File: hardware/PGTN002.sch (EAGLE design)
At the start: 25 parts, among them J1 DCJ0202DCJ0202

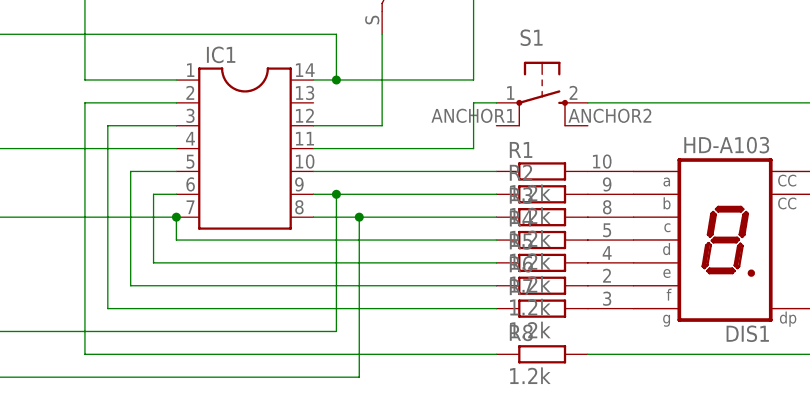
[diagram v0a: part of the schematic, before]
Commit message: Fixed MISO and SCK connection between ATTINY44 and ISP10 socket swapped
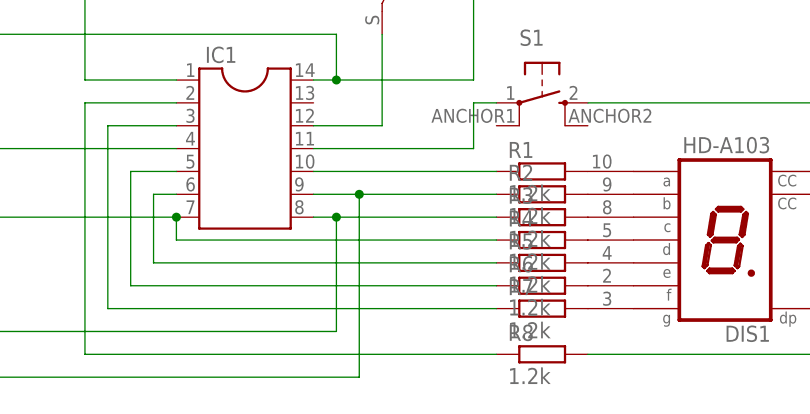
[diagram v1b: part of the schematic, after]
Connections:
- net N$10: now also IC1.8, R3.1; no longer IC1.9, R2.1
- net N$11: now also IC1.9, R2.1; no longer IC1.8, R3.1
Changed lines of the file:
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@@
 <grid distance="0.1" unitdist="inch" unit="inch" style="lines" multiple="1" display="no" altdistance="0.01" altunitdist="inch" altunit="inch"/>
 <layers>
-<layer number="1" name="Top" color="4" fill="1" visible="yes" active="no"/>
-<layer number="16" name="Bottom" color="1" fill="1" visible="yes" active="no"/>
-<layer number="17" name="Pads" color="2" fill="1" visible="yes" active="no"/>
-<layer number="18" name="Vias" color="2" fill="1" visible="yes" active="no"/>
-<layer number="19" name="Unrouted" color="6" fill="1" visible="yes" active="no"/>
-<layer number="20" name="Dimension" color="15" fill="1" visible="yes" active="no"/>
-<layer number="21" name="tPlace" color="7" fill="1" visible="yes" active="no"/>
-<layer number="22" name="bPlace" color="7" fill="1" visible="yes" active="no"/>
-<layer number="23" name="tOrigins" color="15" fill="1" visible="yes" active="no"/>
-<layer number="24" name="bOrigins" color="15" fill="1" visible="yes" active="no"/>
-<layer number="25" name="tNames" color="7" fill="1" visible="yes" active="no"/>
-<layer number="26" name="bNames" color="7" fill="1" visible="yes" active="no"/>
-<layer number="27" name="tValues" color="7" fill="1" visible="yes" active="no"/>
-<layer number="28" name="bValues" color="7" fill="1" visible="yes" active="no"/>
+<layer number="1" name="Top" color="4" fill="1" visible="no" active="no"/>
+<layer number="16" name="Bottom" color="1" fill="1" visible="no" active="no"/>
+<layer number="17" name="Pads" color="2" fill="1" visible="no" active="no"/>
+<layer number="18" name="Vias" color="2" fill="1" visible="no" active="no"/>
+<layer number="19" name="Unrouted" color="6" fill="1" visible="no" active="no"/>
+<layer number="20" name="Dimension" color="15" fill="1" visible="no" active="no"/>
+<layer number="21" name="tPlace" color="7" fill="1" visible="no" active="no"/>
+<layer number="22" name="bPlace" color="7" fill="1" visible="no" active="no"/>
+<layer number="23" name="tOrigins" color="15" fill="1" visible="no" active="no"/>
+<layer number="24" name="bOrigins" color="15" fill="1" visible="no" active="no"/>
+<layer number="25" name="tNames" color="7" fill="1" visible="no" active="no"/>
+<layer number="26" name="bNames" color="7" fill="1" visible="no" active="no"/>
+<layer number="27" name="tValues" color="7" fill="1" visible="no" active="no"/>
+<layer number="28" name="bValues" color="7" fill="1" visible="no" active="no"/>
 <layer number="29" name="tStop" color="7" fill="3" visible="no" active="no"/>
 <layer number="30" name="bStop" color="7" fill="6" visible="no" active="no"/>
@@
 <layer number="35" name="tGlue" color="7" fill="4" visible="no" active="no"/>
 <layer number="36" name="bGlue" color="7" fill="5" visible="no" active="no"/>
-<layer number="37" name="tTest" color="7" fill="1" visible="yes" active="no"/>
-<layer number="38" name="bTest" color="7" fill="1" visible="yes" active="no"/>
+<layer number="37" name="tTest" color="7" fill="1" visible="no" active="no"/>
+<layer number="38" name="bTest" color="7" fill="1" visible="no" active="no"/>
 <layer number="39" name="tKeepout" color="4" fill="11" visible="no" active="no"/>
 <layer number="40" name="bKeepout" color="1" fill="11" visible="no" active="no"/>
@@
 <layer number="44" name="Drills" color="7" fill="1" visible="no" active="no"/>
 <layer number="45" name="Holes" color="7" fill="1" visible="no" active="no"/>
-<layer number="46" name="Milling" color="3" fill="1" visible="yes" active="no"/>
-<layer number="47" name="Measures" color="7" fill="1" visible="yes" active="no"/>
-<layer number="48" name="Document" color="7" fill="1" visible="yes" active="no"/>
-<layer number="49" name="Reference" color="7" fill="1" visible="yes" active="no"/>
-<layer number="50" name="dxf" color="7" fill="1" visible="yes" active="no"/>
-<layer number="51" name="tDocu" color="7" fill="1" visible="yes" active="no"/>
-<layer number="52" name="bDocu" color="7" fill="1" visible="yes" active="no"/>
-<layer number="53" name="tGND_GNDA" color="7" fill="9" visible="yes" active="no"/>
-<layer number="54" name="bGND_GNDA" color="1" fill="9" visible="yes" active="no"/>
-<layer number="56" name="wert" color="7" fill="1" visible="yes" active="no"/>
+<layer number="46" name="Milling" color="3" fill="1" visible="no" active="no"/>
+<layer number="47" name="Measures" color="7" fill="1" visible="no" active="no"/>
+<layer number="48" name="Document" color="7" fill="1" visible="no" active="no"/>
+<layer number="49" name="Reference" color="7" fill="1" visible="no" active="no"/>
+<layer number="50" name="dxf" color="7" fill="1" visible="no" active="no"/>
+<layer number="51" name="tDocu" color="7" fill="1" visible="no" active="no"/>
+<layer number="52" name="bDocu" color="7" fill="1" visible="no" active="no"/>
+<layer number="53" name="tGND_GNDA" color="7" fill="9" visible="no" active="no"/>
+<layer number="54" name="bGND_GNDA" color="1" fill="9" visible="no" active="no"/>
+<layer number="56" name="wert" color="7" fill="1" visible="no" active="no"/>
 <layer number="91" name="Nets" color="2" fill="1" visible="yes" active="yes"/>
 <layer number="92" name="Busses" color="1" fill="1" visible="yes" active="yes"/>
@@
 <net name="N$10" class="0">
 <segment>
+<wire x1="10.16" y1="-7.62" x2="-30.48" y2="-7.62" width="0.1524" layer="91"/>
+<pinref part="MISO" gate="HEADER" pin="3"/>
+<pinref part="R3" gate="G$1" pin="1"/>
+<pinref part="IC1" gate="G$1" pin="8"/>
+<wire x1="7.62" y1="5.08" x2="10.16" y2="5.08" width="0.1524" layer="91"/>
+<wire x1="12.7" y1="5.08" x2="27.94" y2="5.08" width="0.1524" layer="91"/>
+<wire x1="10.16" y1="-7.62" x2="10.16" y2="5.08" width="0.1524" layer="91"/>
+<wire x1="10.16" y1="5.08" x2="12.7" y2="5.08" width="0.1524" layer="91"/>
+<junction x="10.16" y="5.08"/>
+</segment>
+</net>
+<net name="N$11" class="0">
+<segment>
+<wire x1="12.7" y1="-12.7" x2="-30.48" y2="-12.7" width="0.1524" layer="91"/>
+<pinref part="SCK" gate="HEADER" pin="3"/>
+<pinref part="R2" gate="G$1" pin="1"/>
 <pinref part="IC1" gate="G$1" pin="9"/>
-<wire x1="7.62" y1="7.62" x2="10.16" y2="7.62" width="0.1524" layer="91"/>
-<pinref part="R2" gate="G$1" pin="1"/>
-<wire x1="10.16" y1="7.62" x2="27.94" y2="7.62" width="0.1524" layer="91"/>
-<wire x1="10.16" y1="7.62" x2="10.16" y2="-7.62" width="0.1524" layer="91"/>
-<wire x1="10.16" y1="-7.62" x2="-30.48" y2="-7.62" width="0.1524" layer="91"/>
-<junction x="10.16" y="7.62"/>
-<pinref part="MISO" gate="HEADER" pin="3"/>
-</segment>
-</net>
-<net name="N$11" class="0">
-<segment>
-<pinref part="IC1" gate="G$1" pin="8"/>
-<wire x1="7.62" y1="5.08" x2="12.7" y2="5.08" width="0.1524" layer="91"/>
-<pinref part="R3" gate="G$1" pin="1"/>
-<wire x1="12.7" y1="5.08" x2="27.94" y2="5.08" width="0.1524" layer="91"/>
-<wire x1="12.7" y1="5.08" x2="12.7" y2="-12.7" width="0.1524" layer="91"/>
-<wire x1="12.7" y1="-12.7" x2="-30.48" y2="-12.7" width="0.1524" layer="91"/>
-<junction x="12.7" y="5.08"/>
-<pinref part="SCK" gate="HEADER" pin="3"/>
-</segment>
-</net>
+<wire x1="7.62" y1="7.62" x2="12.7" y2="7.62" width="0.1524" layer="91"/>
+<wire x1="12.7" y1="7.62" x2="27.94" y2="7.62" width="0.1524" layer="91"/>
+<wire x1="12.7" y1="-12.7" x2="12.7" y2="7.62" width="0.1524" layer="91"/>
+<junction x="12.7" y="7.62"/>
+</segment>
+</net>
